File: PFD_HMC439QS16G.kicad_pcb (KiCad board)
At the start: 2 copper layers, 108 x 58 mm, 65 parts, among them J1 REF, J2 IN, J3 Error_Out, J4 Supply, J5 JFET/Bias-T, U1 HMC439QS16G, U2 LT3045EMSE, U3 LT3094EMSE, U4 ADA4896-2ARMZ, U5 ADA4896-2ARMZ

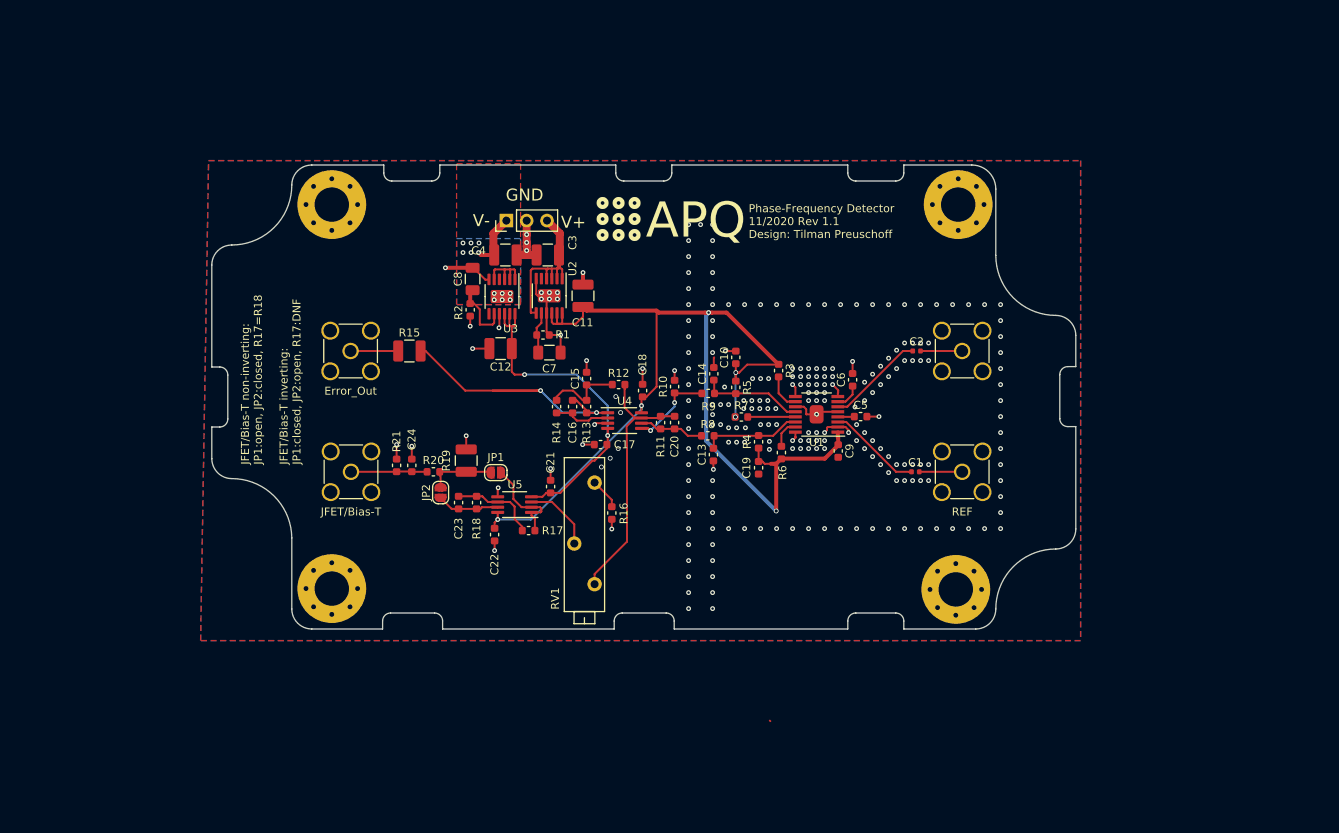
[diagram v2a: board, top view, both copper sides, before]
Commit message: Rev. 1.2
-Divide input signal by 4 using HMC365
-Change board layout to standard eurocard
-Minor changes to 'Fast Out': Optional AC-coupling, optional gain
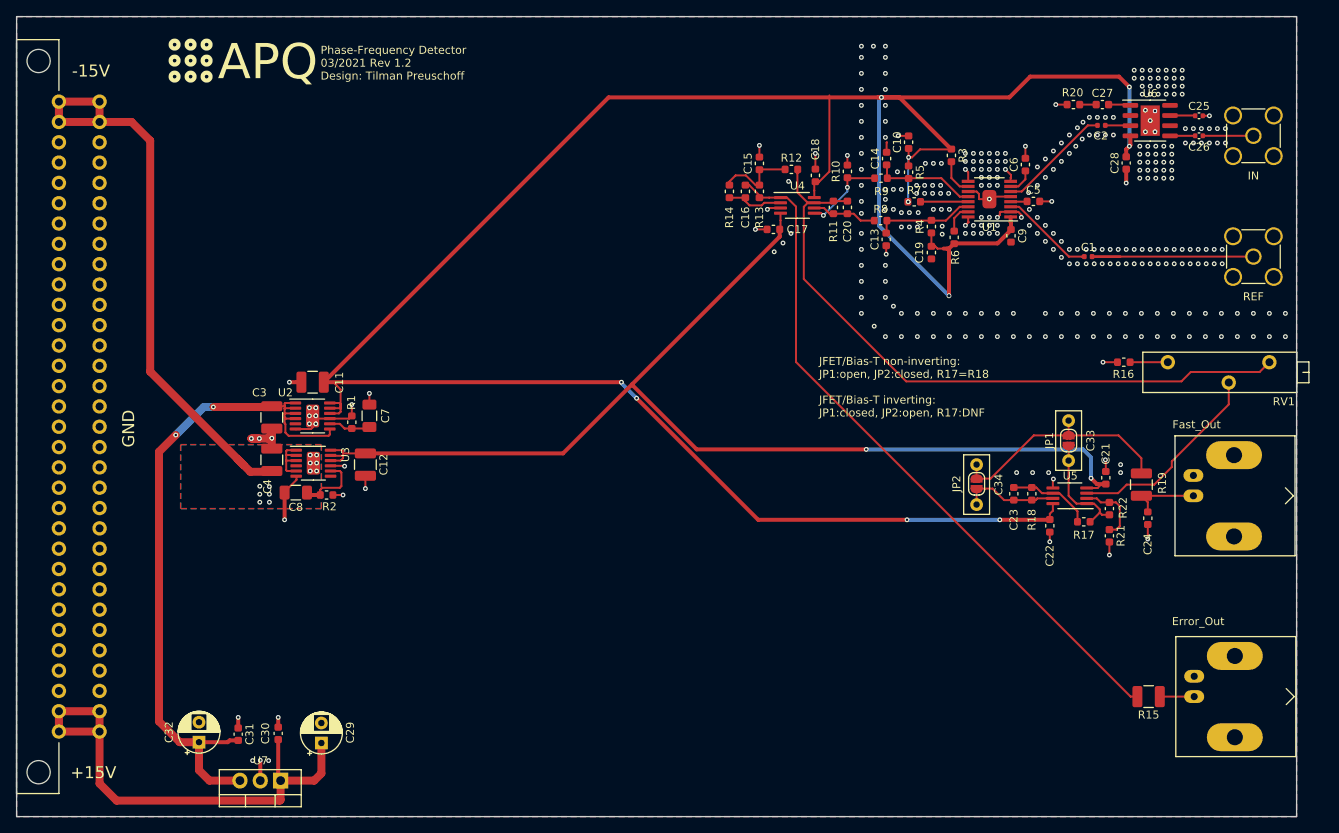
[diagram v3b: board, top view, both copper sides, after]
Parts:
- removed H1, H2, H3, H4: MountingHole_Pad, MountingHole:MountingHole_4.3mm_M4_Pad_Via
- added C25: 100p, Capacitor_SMD:C_0402_1005Metric, F.Cu at (217.8, 62.4)
- added C26: 100p, Capacitor_SMD:C_0402_1005Metric, F.Cu at (217.8, 64.9)
- added C27: 1n, Capacitor_SMD:C_0603_1608Metric, F.Cu at (205.7, 61.0)
- added C28: 100n, Capacitor_SMD:C_0603_1608Metric, F.Cu at (208.7, 68.3)
- added C29: 100u, Capacitor_THT:CP_Radial_D5.0mm_P2.50mm, F.Cu at (108.1, 140.8)
- added C30: 100n, Capacitor_SMD:C_0603_1608Metric, F.Cu at (102.7, 139.6)
- added C31: 100n, Capacitor_SMD:C_0603_1608Metric, F.Cu at (97.7, 139.7)
- added C32: 100u, Capacitor_THT:CP_Radial_D5.0mm_P2.50mm, F.Cu at (92.8, 140.7)
- added C33: DNF, Capacitor_THT:C_Rect_L7.2mm_W3.0mm_P5.00mm_FKS2_FKP2_MKS2_MKP2, F.Cu at (201.5, 100.5)
- added C34: DNF, Capacitor_THT:C_Rect_L7.2mm_W3.0mm_P5.00mm_FKS2_FKP2_MKS2_MKP2, F.Cu at (190.0, 106.0)
- added R22: 0, Capacitor_SMD:C_0603_1608Metric, F.Cu at (206.6, 111.5)
- added U6: HMC365S8G, Package_SO:SOIC-8-1EP_3.9x4.9mm_P1.27mm_EP2.41x3.81mm, F.Cu at (211.7, 63.0)
- added U7: L7809, Package_TO_SOT_THT:TO-220-3_Vertical, F.Cu at (103.0, 145.5)
- C15: value 2.2n -> 560p
- C16: value 560p -> 140p
- C24: value 330p -> DNF
- C9: value 1n -> 100n
- J3: footprint Connector_Coaxial:SMA_Amphenol_901-144_Vertical -> Connector_Coaxial:BNC_Amphenol_B6252HB-NPP3G-50_Horizontal
- J4: value Supply -> C64AC; footprint Connector_PinHeader_2.54mm:PinHeader_1x03_P2.54mm_Vertical -> footprints:Socket_DIN41612-CaseC1-AC-Male-64Pin-2rows
- J5: value JFET/Bias-T -> Fast_Out; footprint Connector_Coaxial:SMA_Amphenol_901-144_Vertical -> Connector_Coaxial:BNC_Amphenol_B6252HB-NPP3G-50_Horizontal
- R19: value 51 -> 49.9
- R20: value 1.2k -> 49.9
- R21: value 51 -> DNF; footprint Resistor_SMD:R_0603_1608Metric -> Capacitor_SMD:C_0603_1608Metric
- moved J3 114.0 mm to (217.2, 135.0), turned to 270 degrees
- moved J5 105.3 mm to (217.1, 109.9), turned to 270 degrees
- moved R15 102.0 mm to (211.5, 135.0), turned to 180 degrees
- moved C24 92.2 mm to (211.4, 112.7), turned to 270 degrees
- moved R20 92.2 mm to (202.1, 61.0), turned to 180 degrees
- moved R21 89.5 mm to (206.6, 114.9)
- moved R19 84.5 mm to (210.6, 108.5)
- moved RV1 73.2 mm to (213.9, 93.2), turned to 180 degrees
- moved JP1 71.7 mm to (201.5, 103.0), turned to 90 degrees
- moved C21 69.4 mm to (206.2, 107.7)
- moved C22 69.4 mm to (199.2, 113.7)
- moved C23 69.4 mm to (194.7, 109.7)
- moved R17 69.4 mm to (203.4, 113.2)
- moved R18 69.4 mm to (196.9, 109.7)
- moved U5 69.4 mm to (201.7, 109.9)
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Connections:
- C2 pad 2: Net-(C2-Pad2) -> Div_out
- C3 pad 1: IN2 -> +9V
- J2 pad 1: Net-(C2-Pad2) -> Net-(C26-Pad2)
- JP1 pad 1: Net-(JP1-Pad1) -> Net-(C33-Pad2)
- JP1 pad 2: Net-(JP1-Pad2) -> Net-(C33-Pad1)
- JP2 pad 2: Net-(JP1-Pad2) -> Net-(C33-Pad1)
- R17 pad 1: Net-(JP1-Pad1) -> Net-(C33-Pad2)
- R19 pad 1: GND -> Net-(C33-Pad1)
- R19 pad 2: Net-(JP1-Pad2) -> Net-(C24-Pad1)
- R20 pad 1: Net-(C24-Pad1) -> Net-(C27-Pad1)
- R20 pad 2: Net-(JP1-Pad2) -> GND
- R21 pad 1: GND -> Net-(R21-Pad1)
- R21 pad 2: Net-(C24-Pad1) -> GND
- U2 pad 1: IN2 -> +9V
- U2 pad 2: IN2 -> +9V
- U2 pad 3: IN2 -> +9V
- U2 pad 4: IN2 -> +9V
- U2 pad 7: IN2 -> +9V
- U5 pad 1: Net-(JP1-Pad1) -> Net-(C33-Pad2)
- U5 pad 2: Net-(JP1-Pad1) -> Net-(R21-Pad1)
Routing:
- net +5V: track 140.9 -> 326.4 mm, vias 6 -> 10
- net -5V: track 43.9 -> 143.1 mm
- net +9V: track 0.00 -> 88.0 mm, vias 0 -> 2
- net IN: track 14.5 -> 80.4 mm
- net +15V: track 0.00 -> 62.2 mm
- net Net-(C20-Pad1): track 32.7 -> 84.0 mm
- net Net-(C16-Pad1): track 36.4 -> 87.0 mm, vias 2 -> 0
- net Net-(C33-Pad1): track 0.00 -> 29.7 mm
- net IN2: track 21.9 -> 0.00 mm
- net Net-(C1-Pad2): track 5.36 -> 24.6 mm
- net Net-(RV1-Pad2): track 8.91 -> 25.5 mm
- net Net-(C33-Pad2): track 0.00 -> 14.8 mm
- net GND: track 72.4 -> 85.6 mm, vias 237 -> 339
- net Net-(JP1-Pad1): track 12.0 -> 0.00 mm
- net Net-(JP1-Pad2): track 8.57 -> 0.00 mm
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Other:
- board size 108 x 58 mm -> 160 x 100 mm
- board text added: "+15V"
- board text added: "-15V"
- board text added: "Phase-Frequency Detector 03/2021 Rev 1.2 Design: Tilman Preuschoff"
- board text removed: "Phase-Frequency Detector 11/2020 Rev 1.1 Design: Tilman Preuschoff"
- board text removed: "V+"
- board text removed: "V-"

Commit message: Fast PD second draft
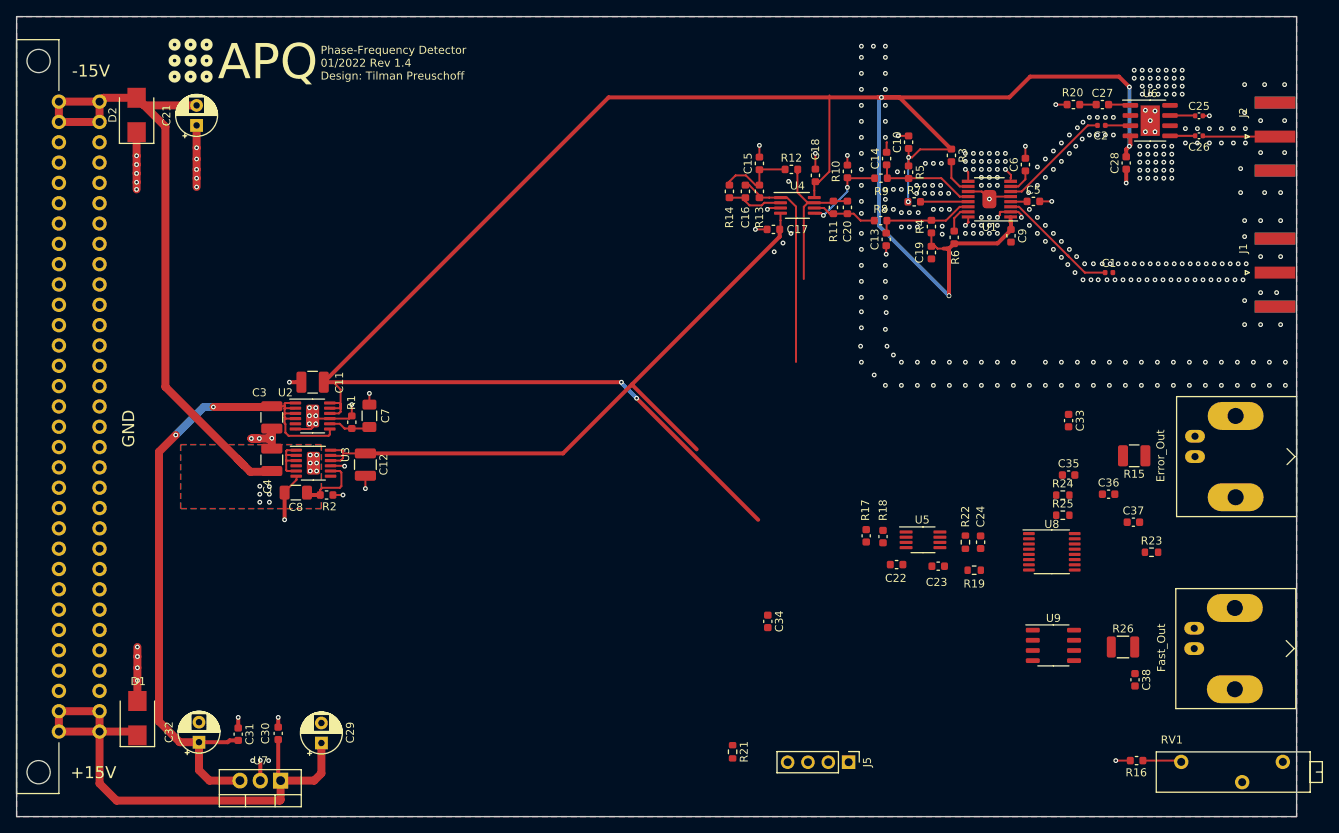
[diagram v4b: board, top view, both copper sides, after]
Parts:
- removed JP1: Inverting, Jumper:SolderJumper-2_P1.3mm_Open_RoundedPad1.0x1.5mm
- removed JP2: Non-Inverting, Jumper:SolderJumper-2_P1.3mm_Open_RoundedPad1.0x1.5mm
- added C35: 1n, Capacitor_SMD:C_0603_1608Metric, F.Cu at (201.5, 107.3)
- added C36: 100n, Capacitor_SMD:C_0603_1608Metric, F.Cu at (206.5, 109.7)
- added C37: 100n, Capacitor_SMD:C_0603_1608Metric, F.Cu at (209.6, 113.2)
- added C38: DNF, Capacitor_SMD:C_0603_1608Metric, F.Cu at (209.8, 132.9)
- added D1: SMB, Diode_SMD:D_SMB, F.Cu at (85.1, 137.7)
- added D2: SMB, Diode_SMD:D_SMB, F.Cu at (85.0, 62.3)
- added J6: Fast_Out, Connector_Coaxial:BNC_Amphenol_B6252HB-NPP3G-50_Horizontal, F.Cu at (217.2, 129.0)
- added R23: 200, Resistor_SMD:R_0603_1608Metric, F.Cu at (211.9, 117.0)
- added R24: 4.7, Resistor_SMD:R_0603_1608Metric, F.Cu at (200.8, 109.8)
- added R25: 200, Resistor_SMD:R_0603_1608Metric, F.Cu at (200.8, 112.3)
- added R26: 49.9, Resistor_SMD:R_1210_3225Metric, F.Cu at (208.3, 128.8)
- added U8: ADG1413, Package_SO:TSSOP-16_4.4x5mm_P0.65mm, F.Cu at (199.4, 116.9)
- added U9: LTC6228xS8, Package_SO:SO-8_3.9x4.9mm_P1.27mm, F.Cu at (199.6, 128.6)
- C13, C14: value 33p -> 15p
- C20: value 560p -> 15p
- C21: value 100n -> 100u; footprint Capacitor_SMD:C_0603_1608Metric -> Capacitor_THT:CP_Radial_D5.0mm_P2.50mm
- C23: value 33p -> 100n
- C24: value DNF -> 15p
- C33, C34: value DNF -> 100n; footprint Capacitor_THT:C_Rect_L7.2mm_W3.0mm_P5.00mm_FKS2_FKP2_MKS2_MKP2 -> Capacitor_SMD:C_0603_1608Metric
- J1, J2: footprint Connector_Coaxial:SMA_Amphenol_901-144_Vertical -> Connector_Coaxial:SMA_Amphenol_132289_EdgeMount
- J5: value Fast_Out -> Switch; footprint Connector_Coaxial:BNC_Amphenol_B6252HB-NPP3G-50_Horizontal -> Connector_PinHeader_2.54mm:PinHeader_1x04_P2.54mm_Vertical
- R10, R11: value 200 -> 380
- R16: value 200 -> 10
- R17, R18: footprint Resistor_SMD:R_0603_1608Metric -> Capacitor_SMD:C_0603_1608Metric
- R19: value 49.9 -> 200; footprint Resistor_SMD:R_1210_3225Metric -> Resistor_SMD:R_0603_1608Metric
- R21: value DNF -> 10k; footprint Capacitor_SMD:C_0603_1608Metric -> Resistor_SMD:R_0603_1608Metric
- R22: value 0 -> 200; footprint Capacitor_SMD:C_0603_1608Metric -> Resistor_SMD:R_0603_1608Metric
- RV1: value 1k -> 500
- U7: value L7809 -> L7808
- moved C21 121.9 mm to (92.5, 63.6)
- moved J5 54.5 mm to (174.0, 143.2)
- moved R21 54.3 mm to (159.5, 141.9)
- moved RV1 50.0 mm to (215.6, 143.2)
- moved R16 49.8 mm to (210.0, 143.0)
- moved C34 32.6 mm to (163.9, 125.6)
- moved R15 30.2 mm to (209.7, 104.9)
- moved J3 30.0 mm to (217.3, 105.0)
- moved R17 27.3 mm to (176.2, 114.9), turned to 90 degrees
- moved R19 23.5 mm to (189.7, 119.2), turned to 0 degrees
- moved C24 21.1 mm to (190.5, 115.7)
- moved C22 19.8 mm to (180.0, 118.5), turned to 180 degrees
- moved R18 19.4 mm to (178.3, 115.0)
- moved U5 19.2 mm to (183.3, 115.4), turned to 0 degrees
- moved R22 18.5 mm to (188.6, 115.7)
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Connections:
- net +9V renamed +8V
- net Net-(C20-Pad1) renamed /Fast PD regulator/error_sig
- C21 pad 1: -5V -> GND
- C21 pad 2: GND -> IN
- C22 pad 1: +5V -> -5V
- C23 pad 1: Net-(C23-Pad1) -> +5V
- C23 pad 2: Net-(C23-Pad2) -> GND
- C24 pad 1: Net-(C24-Pad1) -> S2
- C24 pad 2: GND -> Net-(C24-Pad2)
- C33 pad 1: Net-(C33-Pad1) -> +5V
- C33 pad 2: Net-(C33-Pad2) -> GND
- C34 pad 1: Net-(C33-Pad1) -> -5V
- C34 pad 2: Net-(C23-Pad1) -> GND
- J4 pad A10: Net-(J4-PadA10) -> (no net)
- J4 pad A11: Net-(J4-PadA11) -> (no net)
- J4 pad A12: Net-(J4-PadA12) -> (no net)
- J4 pad A13: Net-(J4-PadA13) -> (no net)
- J4 pad A14: Net-(J4-PadA14) -> (no net)
- J4 pad A18: Net-(J4-PadA18) -> GND
- J4 pad A19: Net-(J4-PadA19) -> (no net)
- J4 pad A20: Net-(J4-PadA20) -> (no net)
- J4 pad A21: Net-(J4-PadA21) -> (no net)
- J4 pad A22: Net-(J4-PadA22) -> (no net)
- J4 pad A23: Net-(J4-PadA23) -> (no net)
- J4 pad A24: Net-(J4-PadA24) -> (no net)
- J4 pad A25: Net-(J4-PadA25) -> (no net)
- J4 pad A26: Net-(J4-PadA26) -> (no net)
- J4 pad A27: Net-(J4-PadA27) -> (no net)
- J4 pad A28: Net-(J4-PadA28) -> (no net)
- J4 pad A29: Net-(J4-PadA29) -> (no net)
- J4 pad A3: Net-(J4-PadA3) -> (no net)
- J4 pad A30: Net-(J4-PadA30) -> (no net)
- J4 pad A4: Net-(J4-PadA4) -> (no net)
- J4 pad A5: Net-(J4-PadA5) -> (no net)
- J4 pad A6: Net-(J4-PadA6) -> (no net)
- J4 pad A7: Net-(J4-PadA7) -> (no net)
- J4 pad A8: Net-(J4-PadA8) -> (no net)
- J4 pad A9: Net-(J4-PadA9) -> (no net)
- J4 pad C10: Net-(J4-PadC10) -> (no net)
- J4 pad C11: Net-(J4-PadC11) -> (no net)
- J4 pad C12: Net-(J4-PadC12) -> (no net)
- J4 pad C13: Net-(J4-PadC13) -> (no net)
- J4 pad C14: Net-(J4-PadC14) -> (no net)
- J4 pad C18: Net-(J4-PadC18) -> GND
- J4 pad C19: Net-(J4-PadC19) -> (no net)
- J4 pad C20: Net-(J4-PadC20) -> (no net)
- J4 pad C21: Net-(J4-PadC21) -> (no net)
- J4 pad C22: Net-(J4-PadC22) -> (no net)
- J4 pad C23: Net-(J4-PadC23) -> (no net)
- J4 pad C24: Net-(J4-PadC24) -> (no net)
- J4 pad C25: Net-(J4-PadC25) -> (no net)
- J4 pad C26: Net-(J4-PadC26) -> (no net)
- J4 pad C27: Net-(J4-PadC27) -> (no net)
- J4 pad C28: Net-(J4-PadC28) -> (no net)
- J4 pad C29: Net-(J4-PadC29) -> (no net)
- J4 pad C3: Net-(J4-PadC3) -> (no net)
- J4 pad C30: Net-(J4-PadC30) -> (no net)
- J4 pad C4: Net-(J4-PadC4) -> (no net)
- J4 pad C5: Net-(J4-PadC5) -> (no net)
- J4 pad C6: Net-(J4-PadC6) -> (no net)
- J4 pad C7: Net-(J4-PadC7) -> (no net)
- J4 pad C8: Net-(J4-PadC8) -> (no net)
- J4 pad C9: Net-(J4-PadC9) -> (no net)
- J5 pad 1: Net-(C24-Pad1) -> Net-(J5-Pad1)
- J5 pad 2: GND -> Net-(J5-Pad2)
- R17 pad 1: Net-(C33-Pad2) -> Net-(R17-Pad1)
- R17 pad 2: Net-(C23-Pad2) -> GND
- R18 pad 1: Net-(C23-Pad2) -> S1
- R18 pad 2: Net-(C23-Pad1) -> Net-(R17-Pad1)
- R19 pad 1: Net-(C33-Pad1) -> S1
- R19 pad 2: Net-(C24-Pad1) -> Net-(C24-Pad2)
- R21 pad 1: Net-(R21-Pad1) -> Net-(J5-Pad1)
- R22 pad 1: Net-(C33-Pad2) -> Net-(C24-Pad2)
- R22 pad 2: Net-(R21-Pad1) -> S2
- U2 pad 5: Net-(U2-Pad5) -> (no net)
- U3 pad 4: Net-(U3-Pad4) -> (no net)
- U3 pad 7: Net-(U3-Pad7) -> (no net)
- U5 pad 1: Net-(C33-Pad2) -> S1
- U5 pad 2: Net-(R21-Pad1) -> Net-(R17-Pad1)
- U5 pad 6: Net-(C23-Pad2) -> Net-(C24-Pad2)
- U5 pad 7: Net-(C23-Pad1) -> S2
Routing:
- net /Fast PD regulator/error_sig: track 84.0 -> 19.5 mm
- net Net-(C16-Pad1): track 87.0 -> 27.0 mm
- net -5V: track 143.1 -> 86.0 mm, vias 2 -> 0
- net +5V: track 326.4 -> 287.8 mm, vias 10 -> 8
- net Net-(C33-Pad1): track 29.7 -> 0.00 mm
- net Net-(RV1-Pad2): track 25.5 -> 0.00 mm
- net Net-(C1-Pad2): track 24.6 -> 0.00 mm
- net Net-(C33-Pad2): track 14.8 -> 0.00 mm
- net GND: track 85.6 -> 99.5 mm, vias 339 -> 378
- net Net-(C23-Pad1): track 12.7 -> 0.00 mm
- net IN: track 80.4 -> 91.8 mm
- net Net-(C23-Pad2): track 10.0 -> 0.00 mm
- net Net-(C24-Pad1): track 8.84 -> 0.00 mm
- net Net-(R21-Pad1): track 8.52 -> 0.00 mm
- net +15V: track 62.2 -> 67.1 mm
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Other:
- net class Default: via_drill 0.4 -> 0.3
- board text added: "Phase-Frequency Detector 01/2022 Rev 1.4 Design: Tilman Preuschoff"
- board text removed: "JFET/Bias-T non-inverting: JP1:open, JP2:closed, R17=R18 JFET/Bias-T inverting: JP1:closed, JP2:open, R17:DNF"
- board text removed: "Phase-Frequency Detector 03/2021 Rev 1.2 Design: Tilman Preuschoff"
